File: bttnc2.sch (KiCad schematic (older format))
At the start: 105 parts, among them K1 MK12C02, P1 ISP, P2 BATTERY, P3 SMA, P4 USB_OTG, P5 U.FL, P6 Serial, Q1 MMBT3904, SW1 SW_PUSH, U1 HC-05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

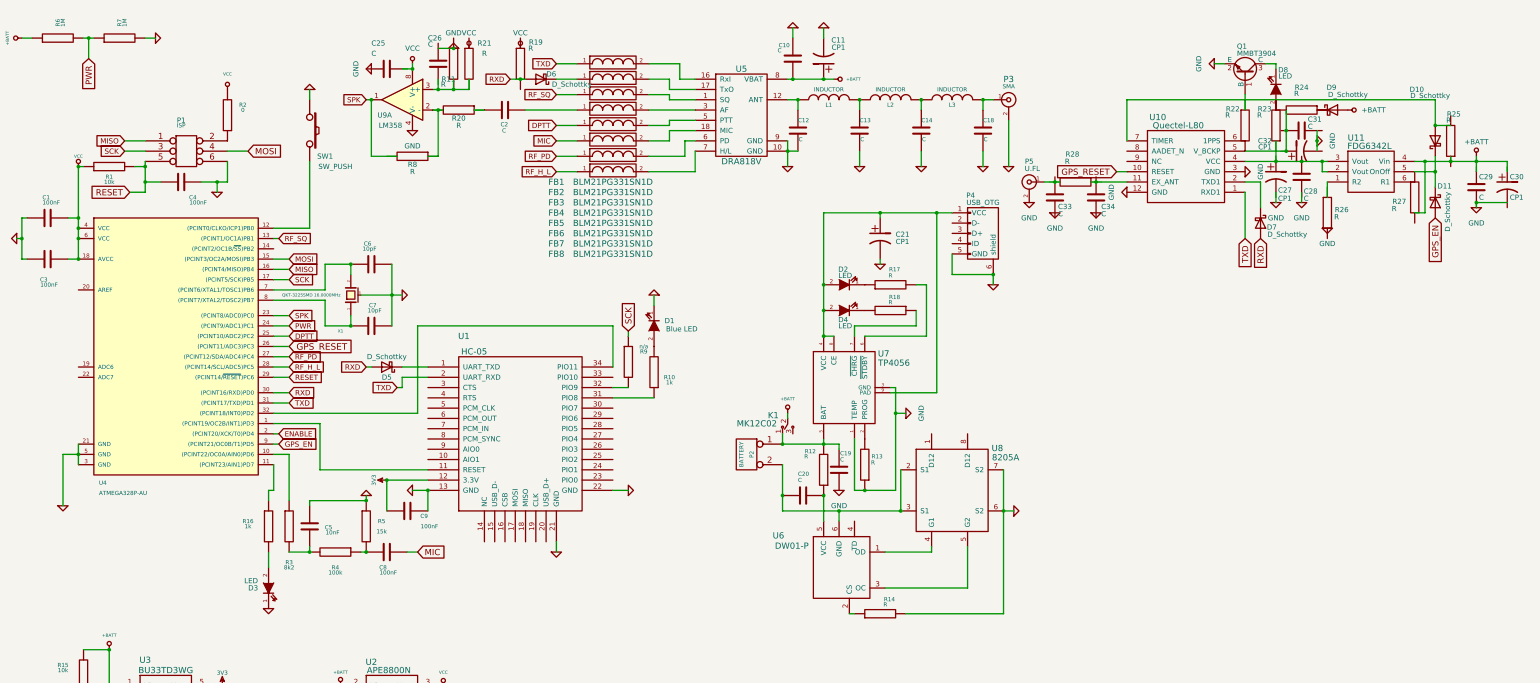
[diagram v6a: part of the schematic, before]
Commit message: Schematics component values update
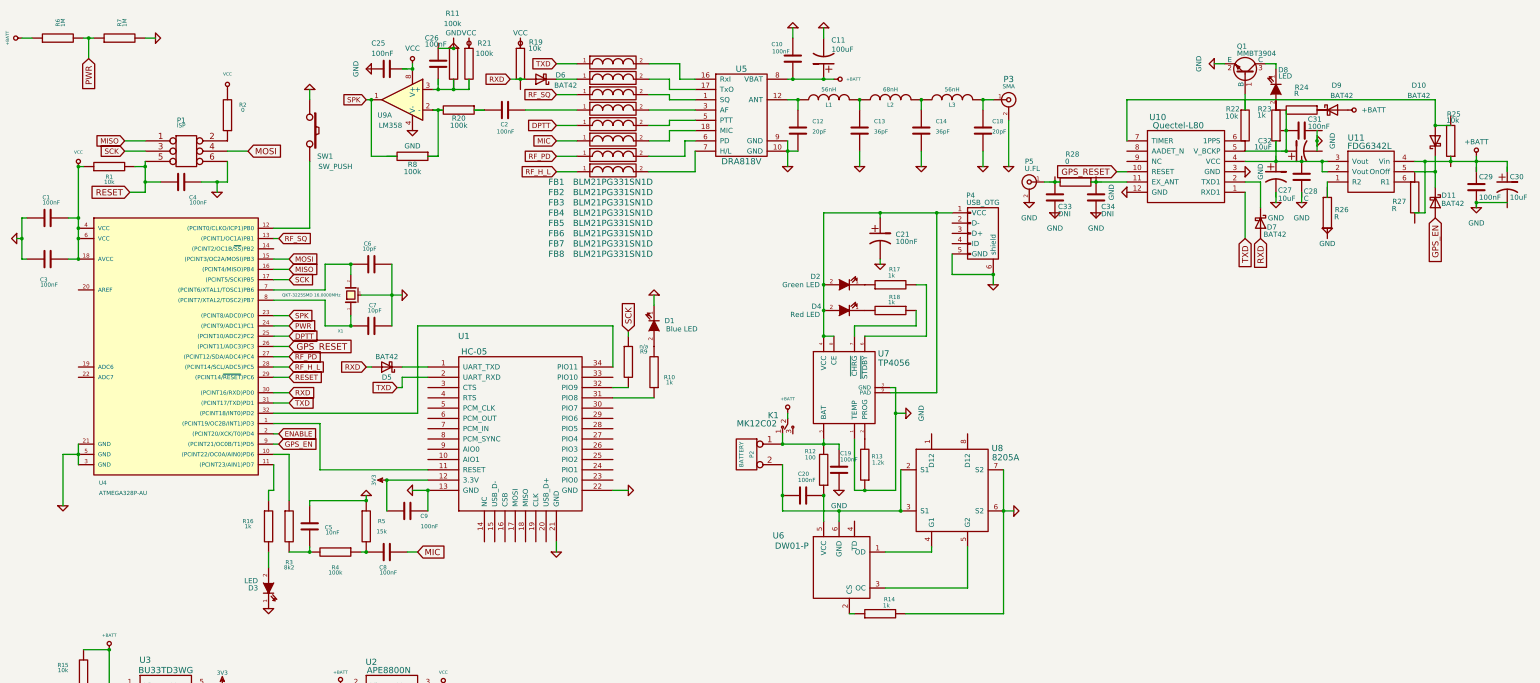
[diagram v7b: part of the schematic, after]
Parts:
- C10, C19, C2, C20, C25, C26, C29, C31: value C -> 100nF
- C11: value CP1 -> 100uF
- C12, C18: value C -> 20pF
- C13, C14: value C -> 36pF
- C21: value CP1 -> 100nF
- C27, C30, C32: value CP1 -> 10uF
- C33, C34: value C -> DNI
- D10, D11, D5, D6, D7, D9: value D_Schottky -> BAT42
- D2: value LED -> Green LED
- D4: value LED -> Red LED
- L1, L3: value INDUCTOR -> 56nH
- L2: value INDUCTOR -> 68nH
- R11, R20, R21, R8: value R -> 100k
- R12: value R -> 100
- R13: value R -> 1.2k
- R14, R17, R18, R23: value R -> 1k
- R19, R22, R25: value R -> 10k
- R28: value R -> 0

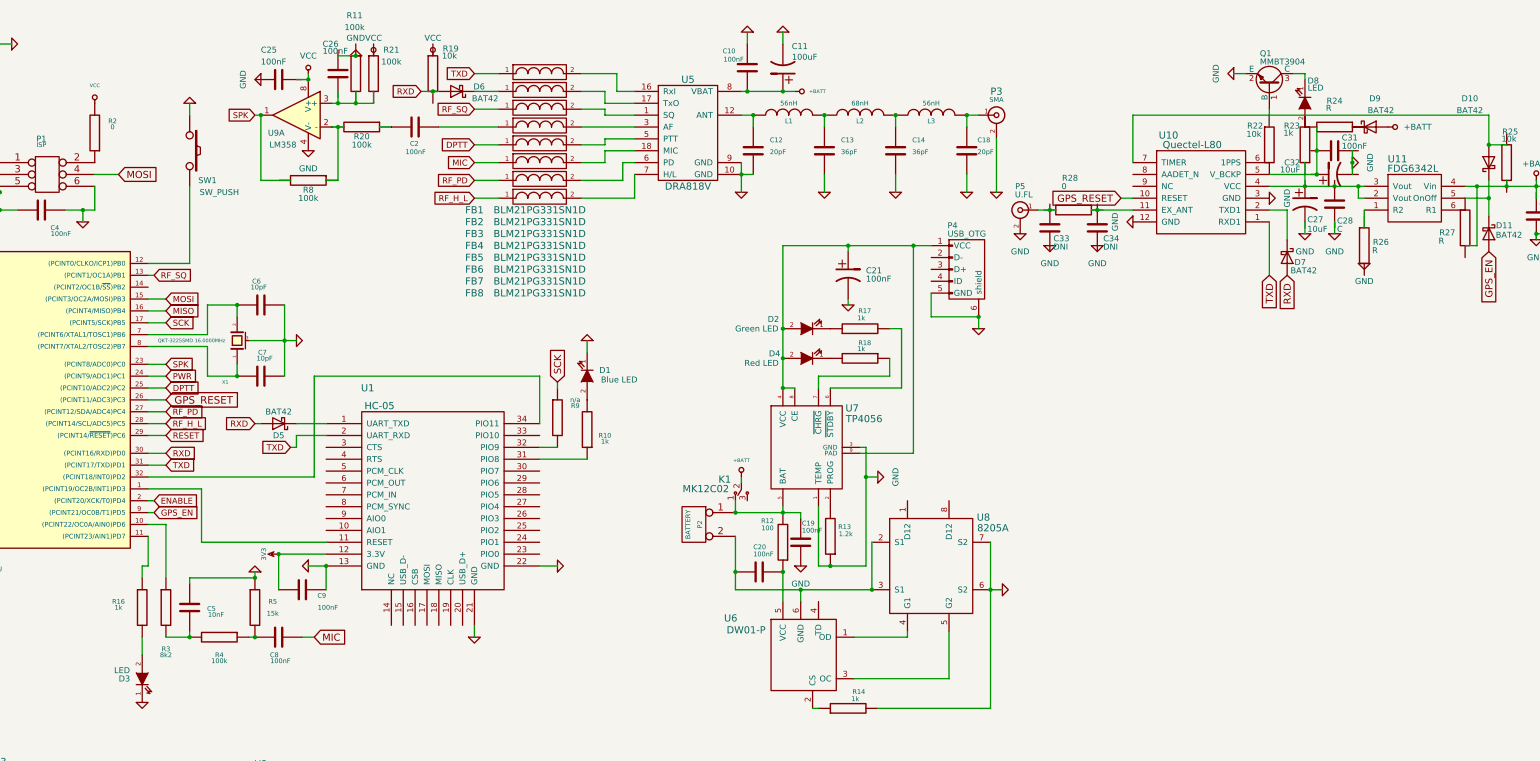
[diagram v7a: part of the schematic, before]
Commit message: Update elements values
This values was changed at device bring up.
We have working hardware configuration.
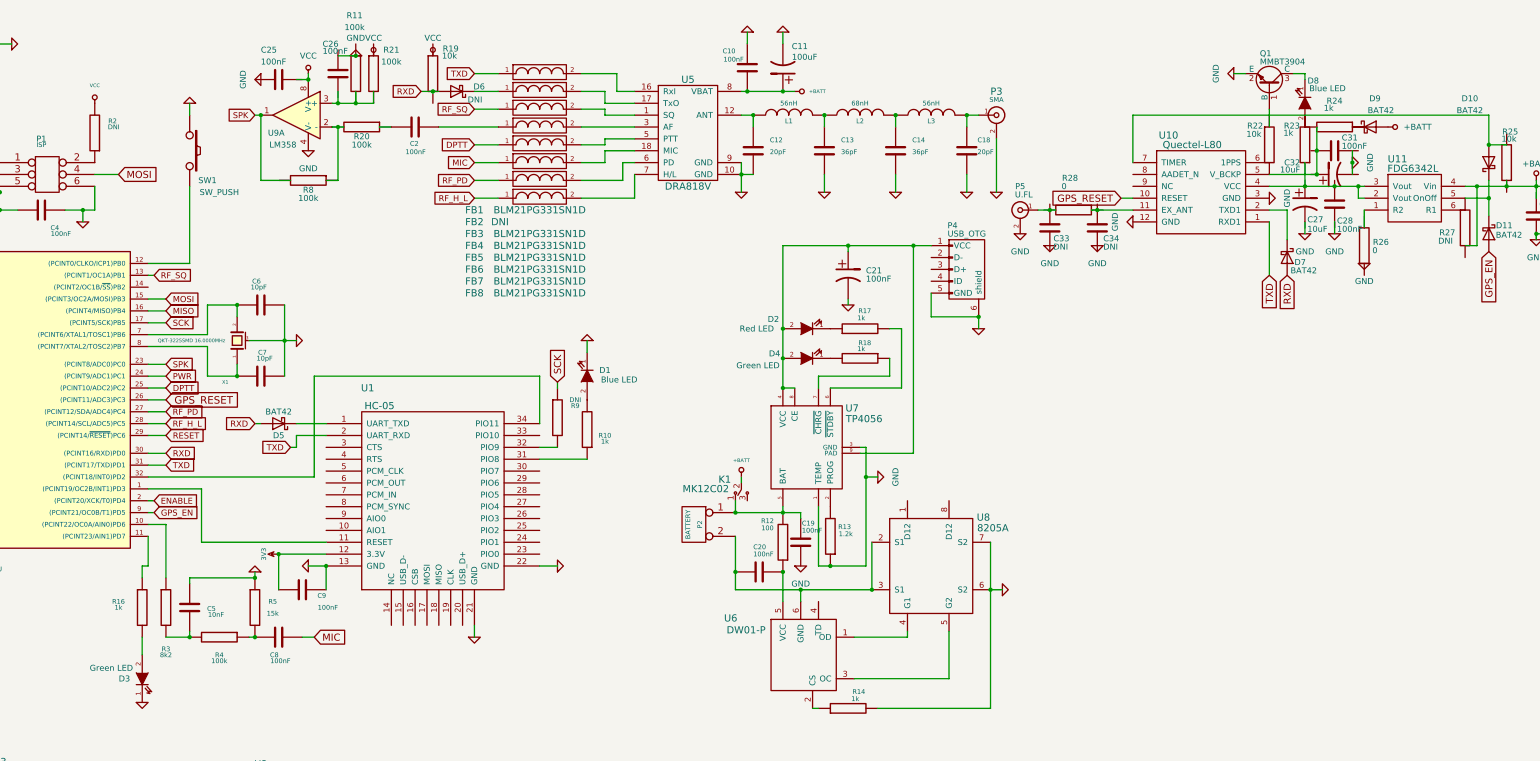
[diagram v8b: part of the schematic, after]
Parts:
- C28: value C -> 100nF
- D2: value Green LED -> Red LED
- D3: value LED -> Green LED
- D4: value Red LED -> Green LED
- D6: value BAT42 -> DNI
- D8: value LED -> Blue LED
- FB2: value BLM21PG331SN1D -> DNI
- R2: value 0 -> DNI
- R24: value R -> 1k
- R26: value R -> 0
- R27: value R -> DNI
- R9: value n/a -> DNI
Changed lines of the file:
@@
 P 3110 3190
 F 0 "R2" H 2960 3090 40  0000 C CNN
-F 1 "0" H 2960 3140 40  0000 C CNN
+F 1 "DNI" H 2950 3140 40  0000 C CNN
 F 2 "Resistors_SMD:R_0805" V 3040 3190 30  0001 C CNN
 F 3 "~" H 3110 3190 30  0000 C CNN
@@
 P 7010 5590
 F 0 "R9" H 7160 5690 40  0000 C CNN
-F 1 "n/a" H 7160 5740 40  0000 C CNN
+F 1 "DNI" H 7160 5740 40  0000 C CNN
 F 2 "Resistors_SMD:R_0805" V 6940 5590 30  0001 C CNN
 F 3 "~" H 7010 5590 30  0000 C CNN
@@
 P 3510 7790
 F 0 "D3" V 3510 7940 50  0000 C CNN
-F 1 "LED" V 3580 7960 50  0000 C CNN
+F 1 "Green LED" V 3600 8050 50  0000 C CNN
 F 2 "LEDs:LED_0805" H 3510 7790 60  0001 C CNN
 F 3 "~" H 3510 7790 60  0000 C CNN
@@
 P 6860 2840
 F 0 "FB2" H 6310 1740 60  0000 C CNN
-F 1 "BLM21PG331SN1D" H 6860 1740 60  0000 C CNN
+F 1 "DNI" H 6525 1740 60  0000 C CNN
 F 2 "Capacitors_SMD:C_0805" H 6860 2840 60  0001 C CNN
 F 3 "~" H 6860 2840 60  0000 C CNN
@@
 P 9110 5090
 F 0 "D4" H 9380 5050 50  0000 C CNN
-F 1 "Red LED" H 9490 5130 50  0000 C CNN
+F 1 "Green LED" H 9520 5150 50  0000 C CNN
 F 2 "LEDs:LED_0805" H 9110 5090 60  0001 C CNN
 F 3 "~" H 9110 5090 60  0000 C CNN
@@
 P 9110 4840
 F 0 "D2" H 9390 4760 50  0000 C CNN
-F 1 "Green LED" H 9530 4840 50  0000 C CNN
+F 1 "Red LED" H 9530 4840 50  0000 C CNN
 F 2 "LEDs:LED_0805" H 9110 4840 60  0001 C CNN
 F 3 "~" H 9110 4840 60  0000 C CNN
@@
 P 6160 2840
 F 0 "D6" H 5970 2800 50  0000 C CNN
-F 1 "BAT42" H 5920 2900 50  0000 C CNN
+F 1 "DNI" H 6005 2910 50  0000 C CNN
 F 2 "Diodes_SMD:MiniMELF_Standard" H 6160 2840 50  0001 C CNN
 F 3 "" H 6160 2840 50  0000 C CNN
@@
 P 13560 3790
 F 0 "C28" H 13580 3650 50  0000 L CNN
-F 1 "C" H 13580 3580 50  0000 L CNN
+F 1 "100nF" H 13580 3580 50  0000 L CNN
 F 2 "Capacitors_SMD:C_0805" H 13598 3640 50  0001 C CNN
 F 3 "" H 13560 3790 50  0000 C CNN
@@
 P 13560 3140
 F 0 "R24" V 13340 3140 50  0000 C CNN
-F 1 "R" V 13400 3090 50  0000 C CNN
+F 1 "1k" V 13400 3090 50  0000 C CNN
 F 2 "Resistors_SMD:R_0805" V 13490 3140 50  0001 C CNN
 F 3 "" H 13560 3140 50  0000 C CNN
@@
 P 13310 2940
 F 0 "D8" V 13120 3010 50  0000 C CNN
-F 1 "LED" V 13180 3030 50  0000 C CNN
+F 1 "Blue LED" V 13185 3130 50  0000 C CNN
 F 2 "LEDs:LED_0805" H 13310 2940 50  0001 C CNN
 F 3 "" H 13310 2940 50  0000 C CNN
@@
 P 13810 4140
 F 0 "R26" H 13950 4170 50  0000 C CNN
-F 1 "R" H 13900 4100 50  0000 C CNN
+F 1 "0" H 13900 4100 50  0000 C CNN
 F 2 "Resistors_SMD:R_0805" V 13740 4140 50  0001 C CNN
 F 3 "" H 13810 4140 50  0000 C CNN
@@
 P 14660 3990
 F 0 "R27" H 14510 3950 50  0000 C CNN
-F 1 "R" H 14460 3880 50  0000 C CNN
+F 1 "DNI" H 14495 3880 50  0000 C CNN
 F 2 "Resistors_SMD:R_0805" V 14590 3990 50  0001 C CNN
 F 3 "" H 14660 3990 50  0000 C CNN
